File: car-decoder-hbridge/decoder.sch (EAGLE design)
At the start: 51 parts, among them U2 RFM69CW, U3 MCP73831, U4 ATMEGA328P, U6 MIC5219 3.3V, Y1 16MHZ

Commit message: some board simplification and isolation of motor speed sensor
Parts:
- removed 2.56V: (no value), wirepad:SMD2
- added R16: 0, SparkFun-Resistors:RESISTOR0603-RES
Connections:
- new net N$1: C4.2, R16.1, R2.2
- net AREF: no longer 2.56V.P
- net GND: no longer C4.2, R2.2
- net OA: now also R16.2
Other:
- moved on the sheet: R14
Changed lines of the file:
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@@
 <part name="R11" library="SparkFun-Resistors" deviceset="RESISTOR" device="0603-RES" value="68"/>
 <part name="LIGHT" library="wirepad" deviceset="SMD2" device=""/>
-<part name="2.56V" library="wirepad" deviceset="SMD2" device=""/>
 <part name="R15" library="SparkFun-Resistors" deviceset="RESISTOR" device="0603-RES" value="68"/>
 <part name="LDR" library="wirepad" deviceset="SMD2" device=""/>
@@
 <part name="R14" library="SparkFun-Resistors" deviceset="RESISTOR" device="0603-RES" value="0"/>
 <part name="SER_B" library="wirepad" deviceset="SMD2" device=""/>
+<part name="GND2" library="SparkFun-Aesthetics" deviceset="GND" device=""/>
+<part name="R16" library="SparkFun-Resistors" deviceset="RESISTOR" device="0603-RES" value="0"/>
 </parts>
 <sheets>
@@
 <instance part="R9" gate="D" x="190.5" y="-20.32"/>
 <instance part="C4" gate="G$1" x="154.94" y="81.28" rot="R90"/>
-<instance part="GND10" gate="1" x="172.72" y="83.82"/>
+<instance part="GND10" gate="1" x="185.42" y="76.2"/>
 <instance part="MOTOR" gate="1" x="223.52" y="96.52" rot="MR0"/>
 <instance part="MOTORGND" gate="1" x="223.52" y="91.44" rot="MR0"/>
@@
 <instance part="R11" gate="G$1" x="190.5" y="50.8"/>
 <instance part="LIGHT" gate="1" x="220.98" y="50.8" rot="MR0"/>
-<instance part="2.56V" gate="1" x="220.98" y="68.58" rot="MR0"/>
 <instance part="R15" gate="G$1" x="190.5" y="58.42"/>
 <instance part="LDR" gate="1" x="220.98" y="63.5" rot="MR0"/>
@@
 <instance part="R13" gate="G$1" x="10.16" y="-20.32"/>
 <instance part="BAT+1" gate="1" x="-17.78" y="137.16"/>
-<instance part="R14" gate="G$1" x="185.42" y="91.44" rot="R180"/>
+<instance part="R14" gate="G$1" x="185.42" y="86.36" rot="R270"/>
 <instance part="SER_B" gate="1" x="-7.62" y="68.58" rot="MR180"/>
+<instance part="GND2" gate="1" x="162.56" y="99.06"/>
+<instance part="R16" gate="G$1" x="172.72" y="91.44"/>
 </instances>
 <busses>
@@
 <wire x1="129.54" y1="104.14" x2="129.54" y2="99.06" width="0.1524" layer="91"/>
 <pinref part="GND9" gate="1" pin="GND"/>
-</segment>
-<segment>
-<pinref part="C4" gate="G$1" pin="2"/>
-<wire x1="157.48" y1="81.28" x2="162.56" y2="81.28" width="0.1524" layer="91"/>
-<wire x1="162.56" y1="81.28" x2="162.56" y2="91.44" width="0.1524" layer="91"/>
-<wire x1="162.56" y1="91.44" x2="157.48" y2="91.44" width="0.1524" layer="91"/>
-<wire x1="162.56" y1="91.44" x2="172.72" y2="91.44" width="0.1524" layer="91"/>
-<junction x="162.56" y="91.44"/>
-<pinref part="GND10" gate="1" pin="GND"/>
-<wire x1="172.72" y1="86.36" x2="172.72" y2="91.44" width="0.1524" layer="91"/>
-<junction x="172.72" y="91.44"/>
-<wire x1="172.72" y1="91.44" x2="180.34" y2="91.44" width="0.1524" layer="91"/>
-<pinref part="MDRIVER" gate="G$1" pin="GND1"/>
-<wire x1="165.1" y1="119.38" x2="162.56" y2="119.38" width="0.1524" layer="91"/>
-<wire x1="162.56" y1="119.38" x2="162.56" y2="104.14" width="0.1524" layer="91"/>
-<pinref part="MDRIVER" gate="G$1" pin="GND"/>
-<wire x1="165.1" y1="104.14" x2="162.56" y2="104.14" width="0.1524" layer="91"/>
-<wire x1="162.56" y1="104.14" x2="162.56" y2="91.44" width="0.1524" layer="91"/>
-<pinref part="R2" gate="G$1" pin="2"/>
-<pinref part="R14" gate="G$1" pin="2"/>
 </segment>
 <segment>
@@
 <wire x1="218.44" y1="-45.72" x2="208.28" y2="-45.72" width="0.1524" layer="91"/>
 </segment>
+<segment>
+<pinref part="GND10" gate="1" pin="GND"/>
+<pinref part="R14" gate="G$1" pin="2"/>
+<wire x1="185.42" y1="78.74" x2="185.42" y2="81.28" width="0.1524" layer="91"/>
+</segment>
+<segment>
+<pinref part="MDRIVER" gate="G$1" pin="GND1"/>
+<wire x1="165.1" y1="119.38" x2="162.56" y2="119.38" width="0.1524" layer="91"/>
+<wire x1="162.56" y1="119.38" x2="162.56" y2="104.14" width="0.1524" layer="91"/>
+<pinref part="MDRIVER" gate="G$1" pin="GND"/>
+<wire x1="165.1" y1="104.14" x2="162.56" y2="104.14" width="0.1524" layer="91"/>
+<pinref part="GND2" gate="1" pin="GND"/>
+<wire x1="162.56" y1="104.14" x2="162.56" y2="101.6" width="0.1524" layer="91"/>
+<junction x="162.56" y="104.14"/>
+</segment>
 </net>
 <net name="AREF" class="0">
-<segment>
-<wire x1="172.72" y1="68.58" x2="218.44" y2="68.58" width="0.1524" layer="91"/>
-<pinref part="2.56V" gate="1" pin="P"/>
-<label x="172.72" y="68.58" size="1.778" layer="95"/>
-</segment>
 <segment>
 <pinref part="U4" gate="G$1" pin="AREF"/>
@@
 <wire x1="193.04" y1="104.14" x2="198.12" y2="104.14" width="0.1524" layer="91"/>
 <wire x1="198.12" y1="104.14" x2="198.12" y2="91.44" width="0.1524" layer="91"/>
+<pinref part="R14" gate="G$1" pin="1"/>
+<wire x1="177.8" y1="91.44" x2="185.42" y2="91.44" width="0.1524" layer="91"/>
+<wire x1="185.42" y1="91.44" x2="198.12" y2="91.44" width="0.1524" layer="91"/>
+<junction x="185.42" y="91.44"/>
 <junction x="198.12" y="91.44"/>
-<wire x1="190.5" y1="91.44" x2="198.12" y2="91.44" width="0.1524" layer="91"/>
-<pinref part="R14" gate="G$1" pin="1"/>
-</segment>
-</net>
+<pinref part="R16" gate="G$1" pin="2"/>
+</segment>
+</net>
+<net name="N$1" class="0">
+<segment>
+<pinref part="R16" gate="G$1" pin="1"/>
+<pinref part="R2" gate="G$1" pin="2"/>
+<pinref part="C4" gate="G$1" pin="2"/>
+<wire x1="157.48" y1="81.28" x2="162.56" y2="81.28" width="0.1524" layer="91"/>
+<wire x1="162.56" y1="81.28" x2="162.56" y2="91.44" width="0.1524" layer="91"/>
+<wire x1="162.56" y1="91.44" x2="157.48" y2="91.44" width="0.1524" layer="91"/>
+<junction x="162.56" y="91.44"/>
+<wire x1="162.56" y1="91.44" x2="167.64" y2="91.44" width="0.1524" layer="91"/>
+</segment>
+</net>

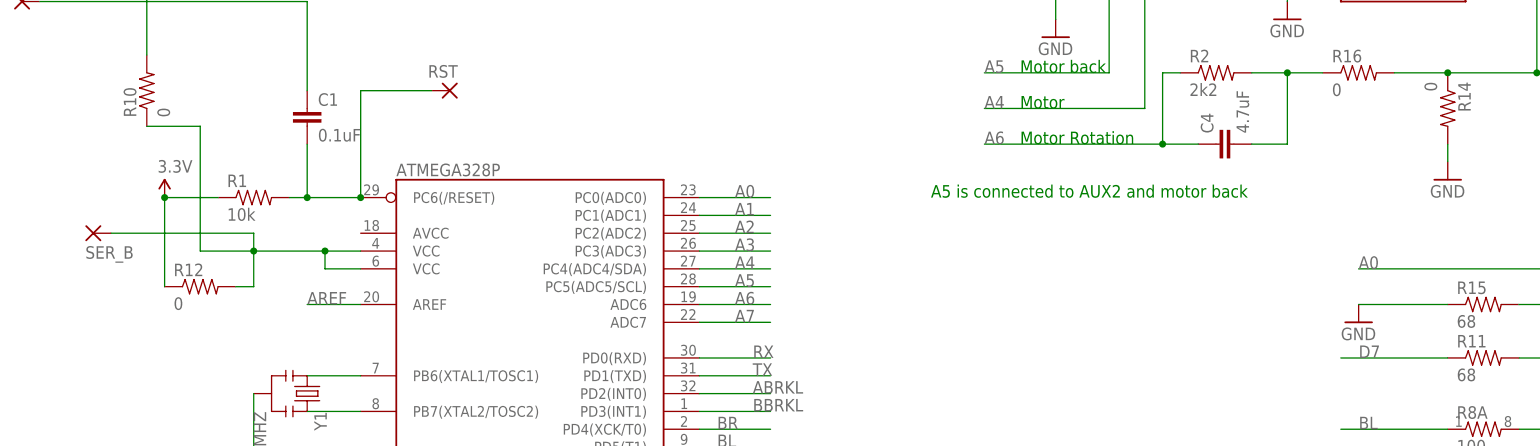
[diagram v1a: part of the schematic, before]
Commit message: New layout for RFM69HC
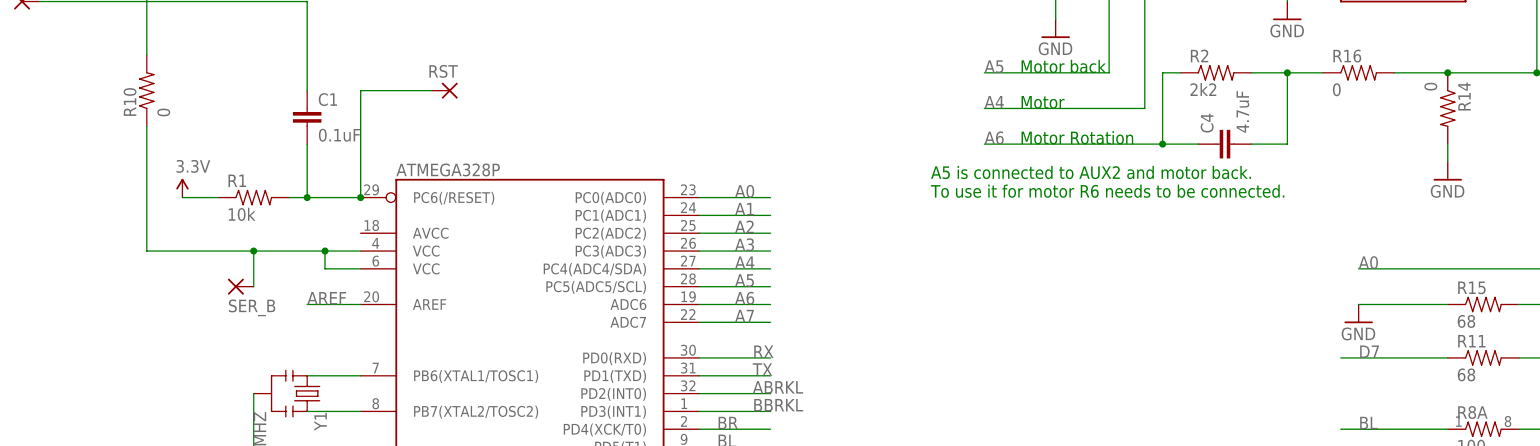
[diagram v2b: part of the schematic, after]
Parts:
- removed R12: 0, SparkFun-Resistors:RESISTOR0603-RES
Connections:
- net N$8: no longer R12.2
- net VCC: no longer R12.1
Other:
- note added: "A5 is connected to AUX2 and motor back. To use it for motor R6 needs to be connected."
- note removed: "A5 is connected to AUX2 and motor back"
- moved on the sheet: SER_B
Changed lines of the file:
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@@
 <part name="R7" library="SparkFun-Resistors" deviceset="RESISTOR" device="0603-RES" value="0"/>
 <part name="R10" library="SparkFun-Resistors" deviceset="RESISTOR" device="0603-RES" value="0"/>
-<part name="R12" library="SparkFun-Resistors" deviceset="RESISTOR" device="0603-RES" value="0"/>
 <part name="R13" library="SparkFun-Resistors" deviceset="RESISTOR" device="0603-RES" value="10k"/>
 <part name="BAT+1" library="wirepad" deviceset="SMD2" device=""/>
@@
 <text x="124.46" y="81.28" size="1.778" layer="91">Motor Rotation</text>
 <text x="124.46" y="91.44" size="1.778" layer="91">Motor back</text>
-<text x="111.76" y="73.66" size="1.778" layer="91">A5 is connected to AUX2 and motor back</text>
+<text x="111.76" y="73.66" size="1.778" layer="91">A5 is connected to AUX2 and motor back.
+To use it for motor R6 needs to be connected.</text>
 </plain>
 <instances>
@@
 <instance part="SER_GND" gate="1" x="-17.78" y="121.92"/>
 <instance part="R1" gate="G$1" x="15.24" y="73.66"/>
-<instance part="VCC4" gate="G$1" x="2.54" y="73.66"/>
+<instance part="VCC4" gate="G$1" x="5.08" y="73.66"/>
 <instance part="SER_DTR" gate="1" x="-17.78" y="101.6"/>
 <instance part="Y1" gate="G$1" x="22.86" y="45.72" rot="R270"/>
@@
 <instance part="R7" gate="G$1" x="152.4" y="106.68"/>
 <instance part="R10" gate="G$1" x="0" y="88.9" rot="R90"/>
-<instance part="R12" gate="G$1" x="7.62" y="60.96"/>
 <instance part="R13" gate="G$1" x="10.16" y="-20.32"/>
 <instance part="BAT+1" gate="1" x="-17.78" y="137.16"/>
 <instance part="R14" gate="G$1" x="185.42" y="86.36" rot="R270"/>
-<instance part="SER_B" gate="1" x="-7.62" y="68.58" rot="MR180"/>
+<instance part="SER_B" gate="1" x="12.7" y="60.96" rot="MR180"/>
 <instance part="GND2" gate="1" x="162.56" y="99.06"/>
 <instance part="R16" gate="G$1" x="172.72" y="91.44"/>
@@
 <segment>
 <pinref part="R1" gate="G$1" pin="1"/>
-<wire x1="10.16" y1="73.66" x2="2.54" y2="73.66" width="0.1524" layer="91"/>
+<wire x1="10.16" y1="73.66" x2="5.08" y2="73.66" width="0.1524" layer="91"/>
 <pinref part="VCC4" gate="G$1" pin="VCC"/>
-<pinref part="R12" gate="G$1" pin="1"/>
-<wire x1="2.54" y1="60.96" x2="2.54" y2="73.66" width="0.1524" layer="91"/>
-<junction x="2.54" y="73.66"/>
 </segment>
 <segment>
@@
 <junction x="25.4" y="66.04"/>
 <wire x1="25.4" y1="66.04" x2="15.24" y2="66.04" width="0.1524" layer="91"/>
-<wire x1="15.24" y1="66.04" x2="7.62" y2="66.04" width="0.1524" layer="91"/>
+<wire x1="15.24" y1="66.04" x2="0" y2="66.04" width="0.1524" layer="91"/>
 <junction x="15.24" y="66.04"/>
-<wire x1="15.24" y1="60.96" x2="15.24" y2="66.04" width="0.1524" layer="91"/>
-<pinref part="R12" gate="G$1" pin="2"/>
-<wire x1="12.7" y1="60.96" x2="15.24" y2="60.96" width="0.1524" layer="91"/>
-<wire x1="7.62" y1="66.04" x2="7.62" y2="83.82" width="0.1524" layer="91"/>
+<wire x1="0" y1="66.04" x2="0" y2="83.82" width="0.1524" layer="91"/>
 <pinref part="R10" gate="G$1" pin="1"/>
-<wire x1="7.62" y1="83.82" x2="0" y2="83.82" width="0.1524" layer="91"/>
-<wire x1="15.24" y1="66.04" x2="15.24" y2="68.58" width="0.1524" layer="91"/>
 <pinref part="SER_B" gate="1" pin="P"/>
-<wire x1="15.24" y1="68.58" x2="-5.08" y2="68.58" width="0.1524" layer="91"/>
+<wire x1="15.24" y1="66.04" x2="15.24" y2="60.96" width="0.1524" layer="91"/>
 </segment>
 </net>
@@
 </schematic>
 </drawing>
+<compatibility>
+<note version="6.3" minversion="6.2.2" severity="warning">
+Since Version 6.2.2 text objects can contain more than one line,
+which will not be processed correctly with this version.
+</note>
+</compatibility>
 </eagle>
